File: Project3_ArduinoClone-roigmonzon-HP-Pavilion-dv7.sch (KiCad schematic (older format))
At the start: 13 parts, among them U1 24LC1025, U2 24LC1025, U3 DS1337_v1, U4 ATMEGA328P-AU, Y1 Crystal 32 MHz, Y2 Crystal 16 MHz

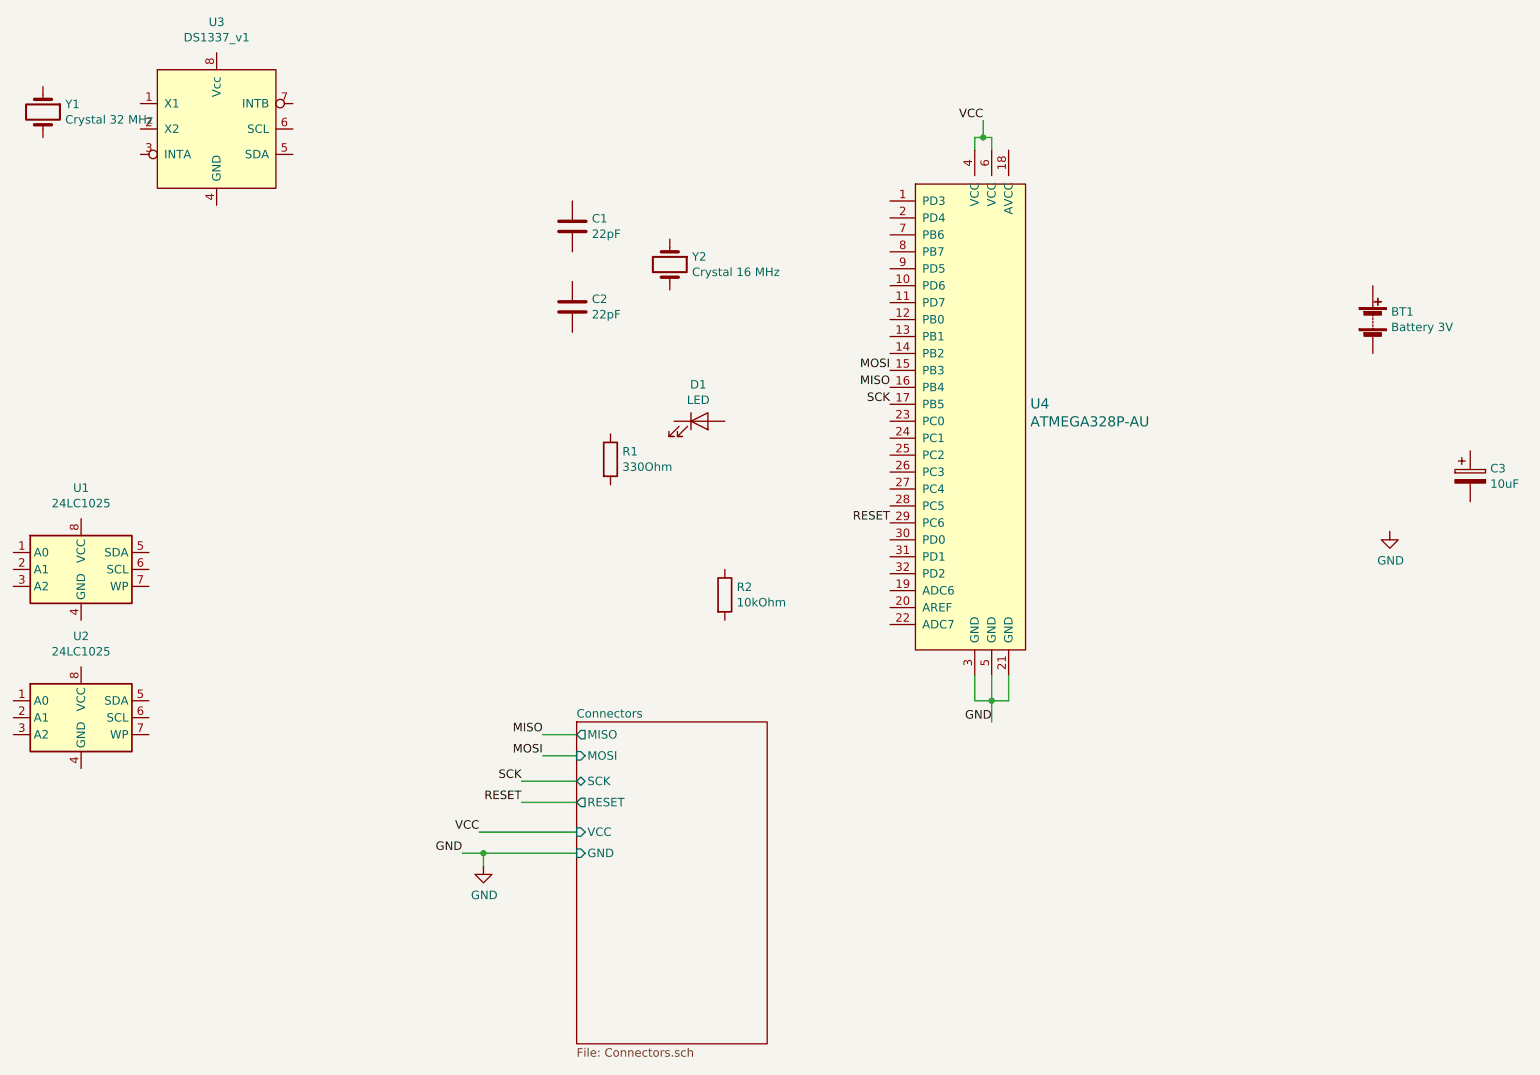
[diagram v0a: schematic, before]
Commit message: Place labels on connectors sheet & wire
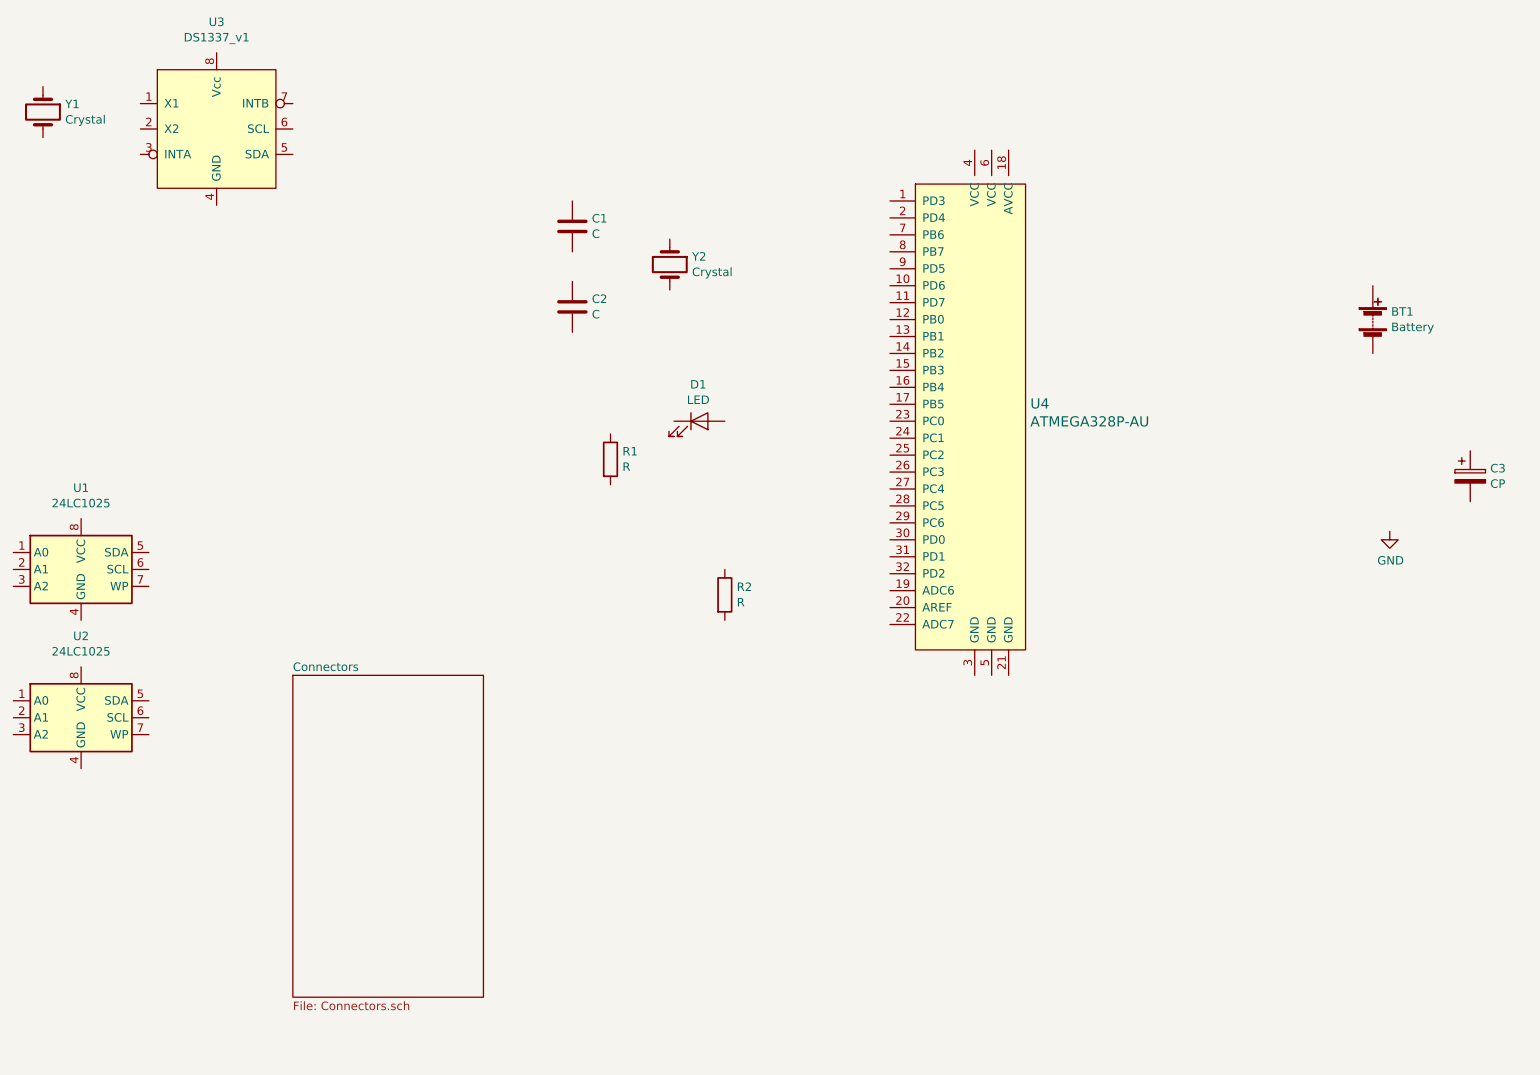
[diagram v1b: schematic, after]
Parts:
- BT1: value Battery 3V -> Battery; footprint Connector_PinHeader_2.54mm:PinHeader_1x02_P2.54mm_Vertical -> (none)
- C1, C2: value 22pF -> C; footprint Capacitor_SMD:C_0805_2012Metric_Pad1.15x1.40mm_HandSolder -> (none)
- C3: value 10uF -> CP; footprint Capacitor_SMD:C_0805_2012Metric_Pad1.15x1.40mm_HandSolder -> (none)
- D1: footprint LED_SMD:LED_0805_2012Metric_Pad1.15x1.40mm_HandSolder -> (none)
- R1: value 330Ohm -> R; footprint Resistor_SMD:R_0805_2012Metric_Pad1.15x1.40mm_HandSolder -> (none)
- R2: value 10kOhm -> R; footprint Resistor_SMD:R_0805_2012Metric_Pad1.15x1.40mm_HandSolder -> (none)
- U1, U2: footprint Package_SO:SOIJ-8_5.3x5.3mm_P1.27mm -> (none)
- U3: footprint Package_SO:SO-8_5.3x6.2mm_P1.27mm -> (none)
- Y1: value Crystal 32 MHz -> Crystal; footprint Crystal:Crystal_SMD_MicroCrystal_CC7V-T1A-2Pin_3.2x1.5mm_HandSoldering -> (none)
- Y2: value Crystal 16 MHz -> Crystal; footprint Crystal:Crystal_SMD_5032-2Pin_5.0x3.2mm_HandSoldering -> (none)
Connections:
- net GND: no longer U4.21 (GND), U4.3 (GND), U4.5 (GND)
- net MISO: no longer names the net of U4.16 (PB4)
- net MOSI: no longer names the net of U4.15 (PB3)
- net RESET: no longer names the net of U4.29 (PC6)
- net SCK: no longer names the net of U4.17 (PB5)
- net VCC: no longer names the net of U4.4 (VCC)
- net VCC: no longer U4.6 (VCC)
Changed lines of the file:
@@
 P 9450 2975
 F 0 "BT1" H 9558 3021 50  0000 L CNN
-F 1 "Battery 3V" H 9558 2930 50  0000 L CNN
-F 2 "Connector_PinHeader_2.54mm:PinHeader_1x02_P2.54mm_Vertical" V 9450 3035 50  0001 C CNN
+F 1 "Battery" H 9558 2930 50  0000 L CNN
+F 2 "" V 9450 3035 50  0001 C CNN
 F 3 "~" V 9450 3035 50  0001 C CNN
 	1    9450 2975
@@
 P 4725 2425
 F 0 "C1" H 4840 2471 50  0000 L CNN
-F 1 "22pF" H 4840 2380 50  0000 L CNN
-F 2 "Capacitor_SMD:C_0805_2012Metric_Pad1.15x1.40mm_HandSolder" H 4763 2275 50  0001 C CNN
+F 1 "C" H 4840 2380 50  0000 L CNN
+F 2 "" H 4763 2275 50  0001 C CNN
 F 3 "~" H 4725 2425 50  0001 C CNN
 	1    4725 2425
@@
 P 4725 2900
 F 0 "C2" H 4840 2946 50  0000 L CNN
-F 1 "22pF" H 4840 2855 50  0000 L CNN
-F 2 "Capacitor_SMD:C_0805_2012Metric_Pad1.15x1.40mm_HandSolder" H 4763 2750 50  0001 C CNN
+F 1 "C" H 4840 2855 50  0000 L CNN
+F 2 "" H 4763 2750 50  0001 C CNN
 F 3 "~" H 4725 2900 50  0001 C CNN
 	1    4725 2900
@@
 P 10025 3900
 F 0 "C3" H 10143 3946 50  0000 L CNN
-F 1 "10uF" H 10143 3855 50  0000 L CNN
-F 2 "Capacitor_SMD:C_0805_2012Metric_Pad1.15x1.40mm_HandSolder" H 10063 3750 50  0001 C CNN
+F 1 "CP" H 10143 3855 50  0000 L CNN
+F 2 "" H 10063 3750 50  0001 C CNN
 F 3 "~" H 10025 3900 50  0001 C CNN
 	1    10025 3900
@@
 F 0 "D1" H 5468 3791 50  0000 C CNN
 F 1 "LED" H 5468 3700 50  0000 C CNN
-F 2 "LED_SMD:LED_0805_2012Metric_Pad1.15x1.40mm_HandSolder" H 5475 3575 50  0001 C CNN
+F 2 "" H 5475 3575 50  0001 C CNN
 F 3 "~" H 5475 3575 50  0001 C CNN
 	1    5475 3575
@@
 P 4950 3800
 F 0 "R1" H 5020 3846 50  0000 L CNN
-F 1 "330Ohm" H 5020 3755 50  0000 L CNN
-F 2 "Resistor_SMD:R_0805_2012Metric_Pad1.15x1.40mm_HandSolder" V 4880 3800 50  0001 C CNN
+F 1 "R" H 5020 3755 50  0000 L CNN
+F 2 "" V 4880 3800 50  0001 C CNN
 F 3 "~" H 4950 3800 50  0001 C CNN
 	1    4950 3800
@@
 P 5625 4600
 F 0 "R2" H 5695 4646 50  0000 L CNN
-F 1 "10kOhm" H 5695 4555 50  0000 L CNN
-F 2 "Resistor_SMD:R_0805_2012Metric_Pad1.15x1.40mm_HandSolder" V 5555 4600 50  0001 C CNN
+F 1 "R" H 5695 4555 50  0000 L CNN
+F 2 "" V 5555 4600 50  0001 C CNN
 F 3 "~" H 5625 4600 50  0001 C CNN
 	1    5625 4600
@@
 F 0 "U1" H 1825 4931 50  0000 C CNN
 F 1 "24LC1025" H 1825 4840 50  0000 C CNN
-F 2 "Package_SO:SOIJ-8_5.3x5.3mm_P1.27mm" H 1825 4450 50  0001 C CNN
+F 2 "" H 1825 4450 50  0001 C CNN
 F 3 "http://ww1.microchip.com/downloads/en/DeviceDoc/21941B.pdf" H 1825 4450 50  0001 C CNN
 	1    1825 4450
 	1    0    0    -1
 $EndComp
+$Sheet
+S 3075 5075 1125 1900
+U 5DA33D85
+F0 "Connectors" 50
+F1 "Connectors.sch" 50
+$EndSheet
 $Comp
 L dk_Embedded-Microcontrollers:ATMEGA328P-AU U4
@@
 F 0 "U3" H 2625 2481 50  0000 C CNN
 F 1 "DS1337_v1" H 2625 2390 50  0000 C CNN
-F 2 "Package_SO:SO-8_5.3x6.2mm_P1.27mm" H 2625 1850 50  0001 C CNN
+F 2 "" H 2625 1850 50  0001 C CNN
 F 3 "https://datasheets.maximintegrated.com/en/ds/DS1337-DS1337C.pdf" H 2625 1850 50  0001 C CNN
 	1    2625 1850
@@
 P 1600 1750
 F 0 "Y1" V 1554 1881 50  0000 L CNN
-F 1 "Crystal 32 MHz" V 1645 1881 50  0000 L CNN
-F 2 "Crystal:Crystal_SMD_MicroCrystal_CC7V-T1A-2Pin_3.2x1.5mm_HandSoldering" H 1600 1750 50  0001 C CNN
+F 1 "Crystal" V 1645 1881 50  0000 L CNN
+F 2 "" H 1600 1750 50  0001 C CNN
 F 3 "~" H 1600 1750 50  0001 C CNN
 	1    1600 1750
@@
 P 5300 2650
 F 0 "Y2" V 5254 2781 50  0000 L CNN
-F 1 "Crystal 16 MHz" V 5345 2781 50  0000 L CNN
-F 2 "Crystal:Crystal_SMD_5032-2Pin_5.0x3.2mm_HandSoldering" H 5300 2650 50  0001 C CNN
+F 1 "Crystal" V 5345 2781 50  0000 L CNN
+F 2 "" H 5300 2650 50  0001 C CNN
 F 3 "~" H 5300 2650 50  0001 C CNN
 	1    5300 2650
@@
 F 0 "U2" H 1825 5806 50  0000 C CNN
 F 1 "24LC1025" H 1825 5715 50  0000 C CNN
-F 2 "Package_SO:SOIJ-8_5.3x5.3mm_P1.27mm" H 1825 5325 50  0001 C CNN
+F 2 "" H 1825 5325 50  0001 C CNN
 F 3 "http://ww1.microchip.com/downloads/en/DeviceDoc/21941B.pdf" H 1825 5325 50  0001 C CNN
 	1    1825 5325
@@
 	1    0    0    -1
 $EndComp
-Text Label 4550 5425 2    50   ~ 0
-MISO
-Wire Wire Line
-	4550 5550 4750 5550
-Text Label 6600 3375 2    50   ~ 0
-MISO
-Text Label 4425 5700 2    50   ~ 0
-SCK
-Text Label 4175 6000 2    50   ~ 0
-VCC
-Text Label 4425 5825 2    50   ~ 0
-RESET
-Text Label 4550 5550 2    50   ~ 0
-MOSI
-Text Label 4075 6125 2    50   ~ 0
-GND
-$Sheet
-S 4750 5350 1125 1900
-U 5DA33D85
-F0 "Connectors" 50
-F1 "Connectors.sch" 50
-F2 "MISO" O L 4750 5425 50
-F3 "SCK" B L 4750 5700 50
-F4 "VCC" I L 4750 6000 50
-F5 "RESET" O L 4750 5825 50
-F6 "MOSI" I L 4750 5550 50
-F7 "GND" I L 4750 6125 50
-$EndSheet
-Wire Wire Line
-	4425 5700 4750 5700
-Wire Wire Line
-	4550 5425 4750 5425
-Wire Wire Line
-	4750 5825 4425 5825
-Wire Wire Line
-	4175 6000 4750 6000
-Wire Wire Line
-	4075 6125 4200 6125
-Text Label 7200 5350 2    50   ~ 0
-GND
-Wire Wire Line
-	7100 5225 7100 5075
-Wire Wire Line
-	7100 5225 7200 5225
-Wire Wire Line
-	7300 5225 7300 5075
-Wire Wire Line
-	7200 5075 7200 5225
-Connection ~ 7200 5225
-Wire Wire Line
-	7200 5225 7300 5225
-Wire Wire Line
-	7200 5350 7200 5225
-Text Label 7150 1800 2    50   ~ 0
-VCC
-Wire Wire Line
-	7100 1975 7100 1900
-Wire Wire Line
-	7100 1900 7150 1900
-Wire Wire Line
-	7200 1900 7200 1975
-Connection ~ 7150 1900
-Wire Wire Line
-	7150 1900 7200 1900
-Wire Wire Line
-	7150 1800 7150 1900
-Text Label 6600 3275 2    50   ~ 0
-MOSI
-Text Label 6600 3475 2    50   ~ 0
-SCK
-Text Label 6600 4175 2    50   ~ 0
-RESET
-$Comp
-L power:GND #PWR?
-U 1 1 5DA57C48
-P 4200 6200
-F 0 "#PWR?" H 4200 5950 50  0001 C CNN
-F 1 "GND" H 4205 6027 50  0000 C CNN
-F 2 "" H 4200 6200 50  0001 C CNN
-F 3 "" H 4200 6200 50  0001 C CNN
-	1    4200 6200
-	1    0    0    -1
-$EndComp
-Wire Wire Line
-	4200 6200 4200 6125
-Connection ~ 4200 6125
-Wire Wire Line
-	4200 6125 4750 6125
 $EndSCHEMATC
